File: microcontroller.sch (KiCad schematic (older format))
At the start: 52 parts, among them J3 FH12A-10S-0.5SH55, J4 , J5 Conn_ARM_JTAG_SWD_20, J6 26642801RP2, SW0 SW_Push, SW1 SW_Push, SW2 SW_Push, SW3 SW_Push, SW4 SW_Push, SW5 SW_Push, SW6 SW_Push, U7 EFM32GG942F1024

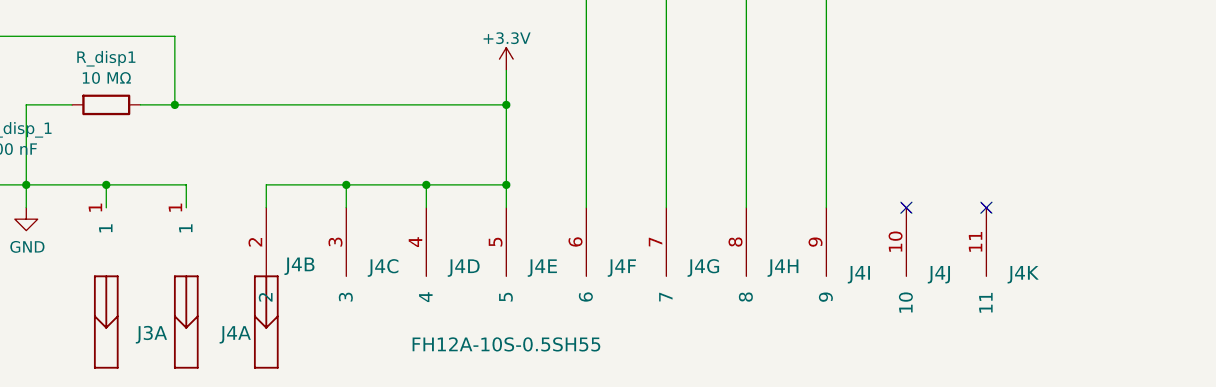
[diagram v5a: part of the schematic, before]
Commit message: Fix LCD connector
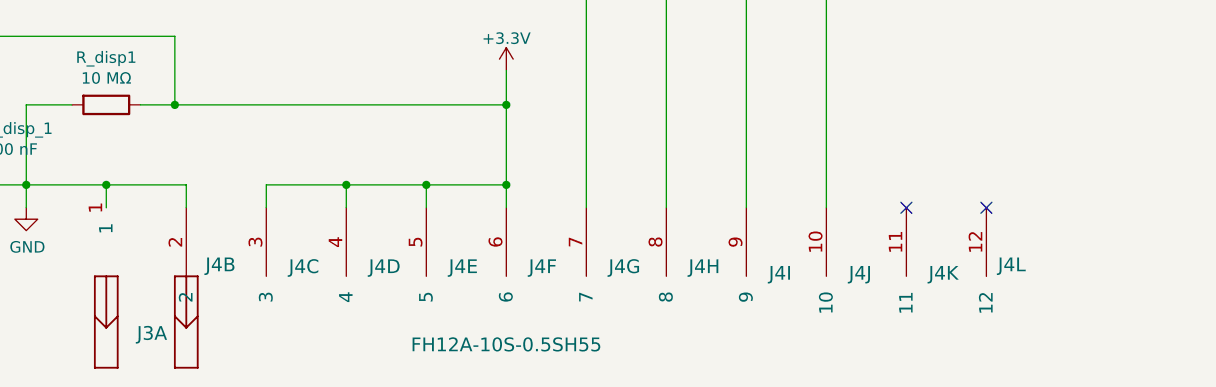
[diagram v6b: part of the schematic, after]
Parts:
- removed unit 1 of J4
- added unit 12 of J4
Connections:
- net +3V3: now also J4.6; no longer J4.2
- net GND: now also J4.2
- net at U7.28 (PD0): now also J4.9; no longer J4.8
- net at U7.30 (PD2): now also J4.10; no longer J4.9
- net at U7.31 (PD3): now also J4.8; no longer J4.7
- net at J6.14: now also J4.7; no longer J4.6
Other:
- moved on the sheet: J4B, J4C, J4D, J4E, J4F, J4G, J4H, J4I, J4J, J4K
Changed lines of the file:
@@
 $Comp
 L LCD:FH12A-10S-0.5SH55 J4
-U 1 1 5D86B092
+U 2 1 5D873ACF
 P 4000 9050
-F 0 "J4" V 3450 9200 60  0000 L CNN
-F 1 " " V 3800 8600 60  0000 L CNN
+F 0 "J4" V 3750 9200 60  0000 C CNN
+F 1 " " V 4200 9050 60  0000 C CNN
 F 2 "CONN10_1X10_DRC_FFC" H 4000 8990 60  0001 C CNN
 F 3 "" H 4000 9050 60  0000 C CNN
-	1    4000 9050
+	2    4000 9050
 	0    1    -1   0
 $EndComp
 $Comp
 L LCD:FH12A-10S-0.5SH55 J4
-U 2 1 5D873ACF
+U 3 1 5D88452F
 P 4350 9050
-F 0 "J4" V 4100 9200 60  0000 C CNN
-F 1 " " V 4550 9050 60  0000 C CNN
+F 0 "J4" V 4092 9148 60  0000 L CNN
+F 1 " " V 4198 9148 60  0000 L CNN
 F 2 "CONN10_1X10_DRC_FFC" H 4350 8990 60  0001 C CNN
 F 3 "" H 4350 9050 60  0000 C CNN
-	2    4350 9050
+	3    4350 9050
 	0    1    -1   0
 $EndComp
 $Comp
 L LCD:FH12A-10S-0.5SH55 J4
-U 3 1 5D88452F
+U 4 1 5D88BAB2
 P 4700 9050
 F 0 "J4" V 4442 9148 60  0000 L CNN
@@
 F 2 "CONN10_1X10_DRC_FFC" H 4700 8990 60  0001 C CNN
 F 3 "" H 4700 9050 60  0000 C CNN
-	3    4700 9050
+	4    4700 9050
 	0    1    -1   0
 $EndComp
 $Comp
 L LCD:FH12A-10S-0.5SH55 J4
-U 4 1 5D88BAB2
+U 5 1 5D891720
 P 5050 9050
 F 0 "J4" V 4792 9148 60  0000 L CNN
@@
 F 2 "CONN10_1X10_DRC_FFC" H 5050 8990 60  0001 C CNN
 F 3 "" H 5050 9050 60  0000 C CNN
-	4    5050 9050
+	5    5050 9050
 	0    1    -1   0
 $EndComp
 $Comp
 L LCD:FH12A-10S-0.5SH55 J4
-U 5 1 5D891720
+U 6 1 5D89776E
 P 5400 9050
 F 0 "J4" V 5142 9148 60  0000 L CNN
@@
 F 2 "CONN10_1X10_DRC_FFC" H 5400 8990 60  0001 C CNN
 F 3 "" H 5400 9050 60  0000 C CNN
-	5    5400 9050
+	6    5400 9050
 	0    1    -1   0
 $EndComp
 $Comp
 L LCD:FH12A-10S-0.5SH55 J4
-U 6 1 5D89776E
+U 7 1 5D89D729
 P 5750 9050
-F 0 "J4" V 5492 9148 60  0000 L CNN
-F 1 " " V 5598 9148 60  0000 L CNN
+F 0 "J4" V 5492 9147 60  0000 L CNN
+F 1 " " V 5598 9147 60  0000 L CNN
 F 2 "CONN10_1X10_DRC_FFC" H 5750 8990 60  0001 C CNN
 F 3 "" H 5750 9050 60  0000 C CNN
-	6    5750 9050
+	7    5750 9050
 	0    1    -1   0
 $EndComp
 $Comp
 L LCD:FH12A-10S-0.5SH55 J4
-U 7 1 5D89D729
+U 8 1 5D8A2C47
 P 6100 9050
 F 0 "J4" V 5842 9147 60  0000 L CNN
@@
 F 2 "CONN10_1X10_DRC_FFC" H 6100 8990 60  0001 C CNN
 F 3 "" H 6100 9050 60  0000 C CNN
-	7    6100 9050
+	8    6100 9050
 	0    1    -1   0
 $EndComp
 $Comp
 L LCD:FH12A-10S-0.5SH55 J4
-U 8 1 5D8A2C47
+U 9 1 5D8AB529
 P 6450 9050
-F 0 "J4" V 6192 9147 60  0000 L CNN
-F 1 " " V 6298 9147 60  0000 L CNN
+F 0 "J4" V 6163 9148 60  0000 L CNN
+F 1 " " V 6269 9148 60  0000 L CNN
 F 2 "CONN10_1X10_DRC_FFC" H 6450 8990 60  0001 C CNN
 F 3 "" H 6450 9050 60  0000 C CNN
-	8    6450 9050
+	9    6450 9050
 	0    1    -1   0
 $EndComp
 $Comp
 L LCD:FH12A-10S-0.5SH55 J4
-U 9 1 5D8AB529
+U 10 1 5D8B1A3C
 P 6800 9050
 F 0 "J4" V 6513 9148 60  0000 L CNN
@@
 F 2 "CONN10_1X10_DRC_FFC" H 6800 8990 60  0001 C CNN
 F 3 "" H 6800 9050 60  0000 C CNN
-	9    6800 9050
+	10   6800 9050
 	0    1    -1   0
 $EndComp
 $Comp
 L LCD:FH12A-10S-0.5SH55 J4
-U 10 1 5D8B1A3C
+U 11 1 5D8B82A9
 P 7150 9050
-F 0 "J4" V 6863 9148 60  0000 L CNN
-F 1 " " V 6969 9148 60  0000 L CNN
+F 0 "J4" V 6863 9147 60  0000 L CNN
+F 1 " " V 6969 9147 60  0000 L CNN
 F 2 "CONN10_1X10_DRC_FFC" H 7150 8990 60  0001 C CNN
 F 3 "" H 7150 9050 60  0000 C CNN
-	10   7150 9050
-	0    1    -1   0
-$EndComp
-$Comp
-L LCD:FH12A-10S-0.5SH55 J4
-U 11 1 5D8B82A9
-P 7500 9050
-F 0 "J4" V 7213 9147 60  0000 L CNN
-F 1 " " V 7319 9147 60  0000 L CNN
-F 2 "CONN10_1X10_DRC_FFC" H 7500 8990 60  0001 C CNN
-F 3 "" H 7500 9050 60  0000 C CNN
-	11   7500 9050
+	11   7150 9050
 	0    1    -1   0
 $EndComp
@@
 Wire Wire Line
 	3300 8950 3300 9050
-Wire Wire Line
-	4000 9050 4000 8950
-Wire Wire Line
-	4000 8950 3650 8950
-Connection ~ 3650 8950
 Wire Wire Line
 	4350 9050 4350 8950
@@
 Wire Wire Line
 	6650 5250 6850 5250
+Connection ~ 3650 8950
+Wire Wire Line
+	4000 8950 3650 8950
+Wire Wire Line
+	4000 9050 4000 8950
+$Comp
+L LCD:FH12A-10S-0.5SH55 J4
+U 12 1 5D9B45F3
+P 7500 9050
+F 0 "J4" V 7250 9000 60  0000 R CNN
+F 1 " " V 7213 8988 60  0000 R CNN
+F 2 "CONN10_1X10_DRC_FFC" H 7500 8990 60  0001 C CNN
+F 3 "" H 7500 9050 60  0000 C CNN
+	12   7500 9050
+	0    -1   -1   0
+$EndComp
 $EndSCHEMATC

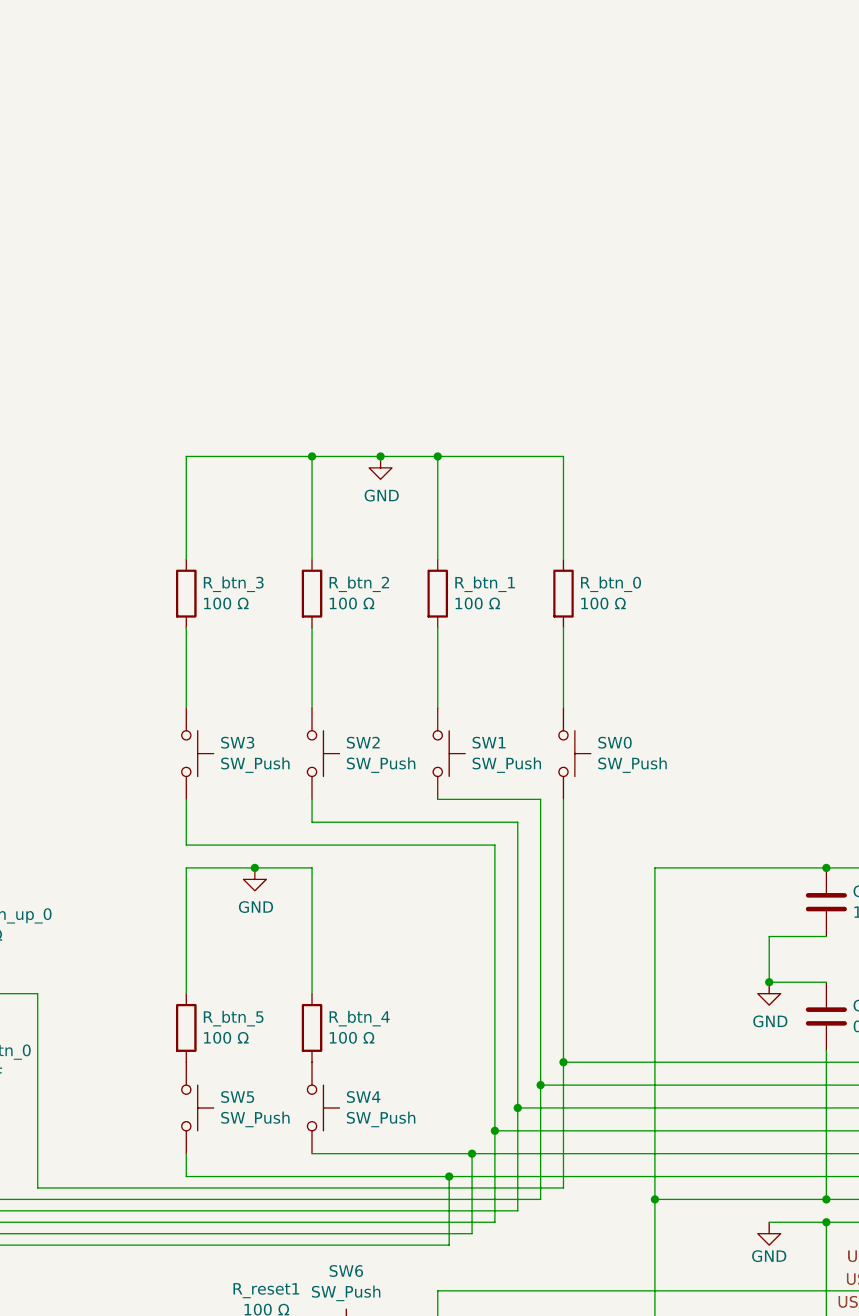
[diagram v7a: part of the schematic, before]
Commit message: Add button schematic and footprint
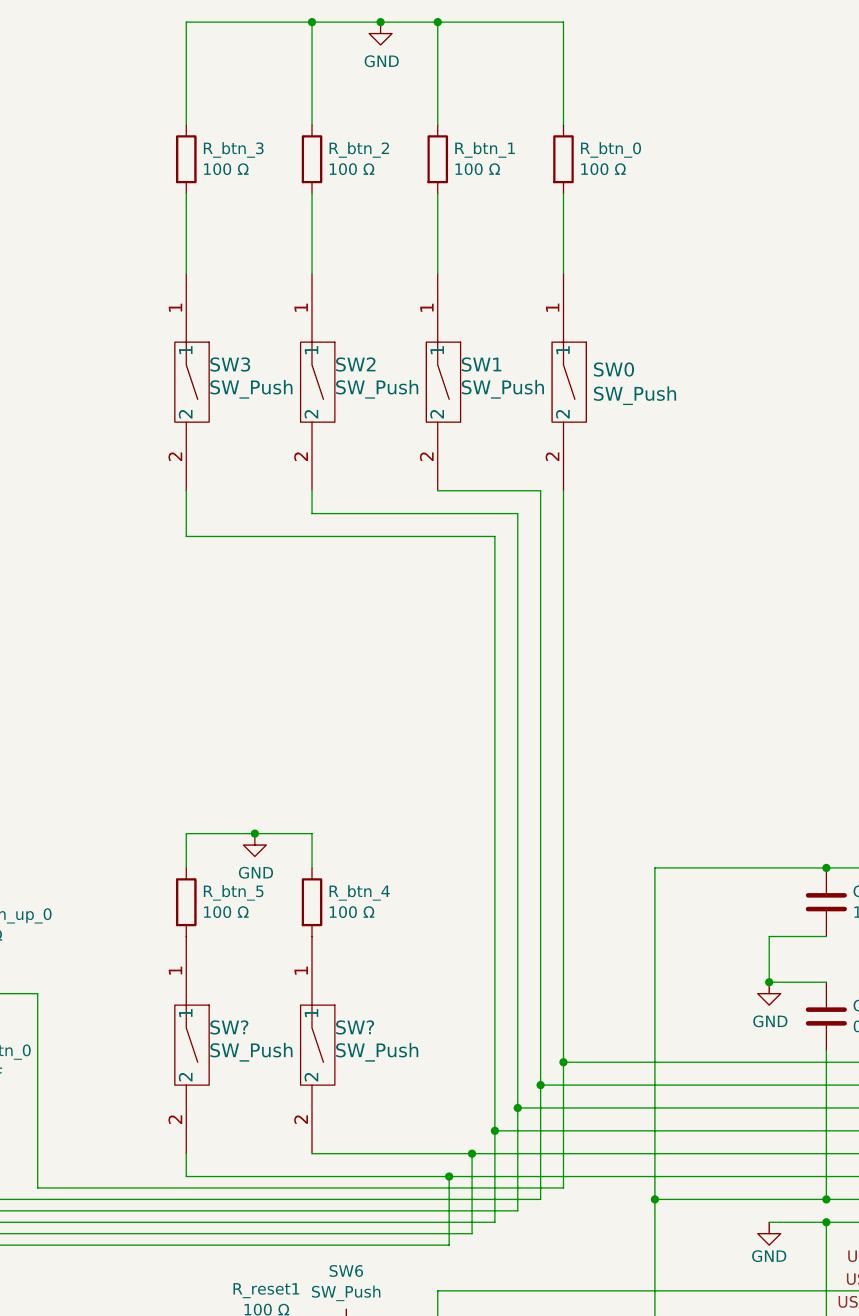
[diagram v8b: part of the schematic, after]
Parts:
- removed SW0, SW1, SW2, SW3, SW4, SW5: SW_Push, symbol Switch:SW_Push
- added SW0, SW1, SW2, SW3, SW? (x2): SW_Push, SWITCH_FSMSMTR, symbol button:FSMSMTR
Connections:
- net at C_btn_0.1, R_btn_up_0.2, U7.1 (PA0): now also SW0.2
- net at C_btn_1.1, R_btn_up_1.2, U7.2 (PA1): now also SW1.2
- net at C_btn_2.1, R_btn_up_2.2, U7.3 (PA2): now also SW2.2
- net at C_btn_3.1, R_btn_up_3.2, U7.4 (PA3): now also SW3.2
- net at C_btn_4.1, R_btn_up_4.2, U7.5 (PA4): now also SW?.2
- net at C_btn_5.1, R_btn_up_5.2, U7.6 (PA5): now also SW?.2
- net at R_btn_0.2: now also SW0.1
- net at R_btn_1.2: now also SW1.1
- net at R_btn_2.2: now also SW2.1
- net at R_btn_3.2: now also SW3.1
- net at R_btn_5.2: now also SW?.1
- net at R_btn_4.2: now also SW?.1
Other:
- moved on the sheet: R_btn_0, R_btn_1, R_btn_2, R_btn_3, R_btn_4, R_btn_5
